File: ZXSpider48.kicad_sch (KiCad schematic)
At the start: 121 parts, among them J1 Barrel_Jack_Switch, J11 EAR/MIC, J12 KB_CONN_05, J14 RESET, J15 ZX_48K_EDGE, J17 ON/OFF, J2 JTAG, J3 9V, J5 ROM_SW, J6 M-DIN KMDGX-9S-BS-1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

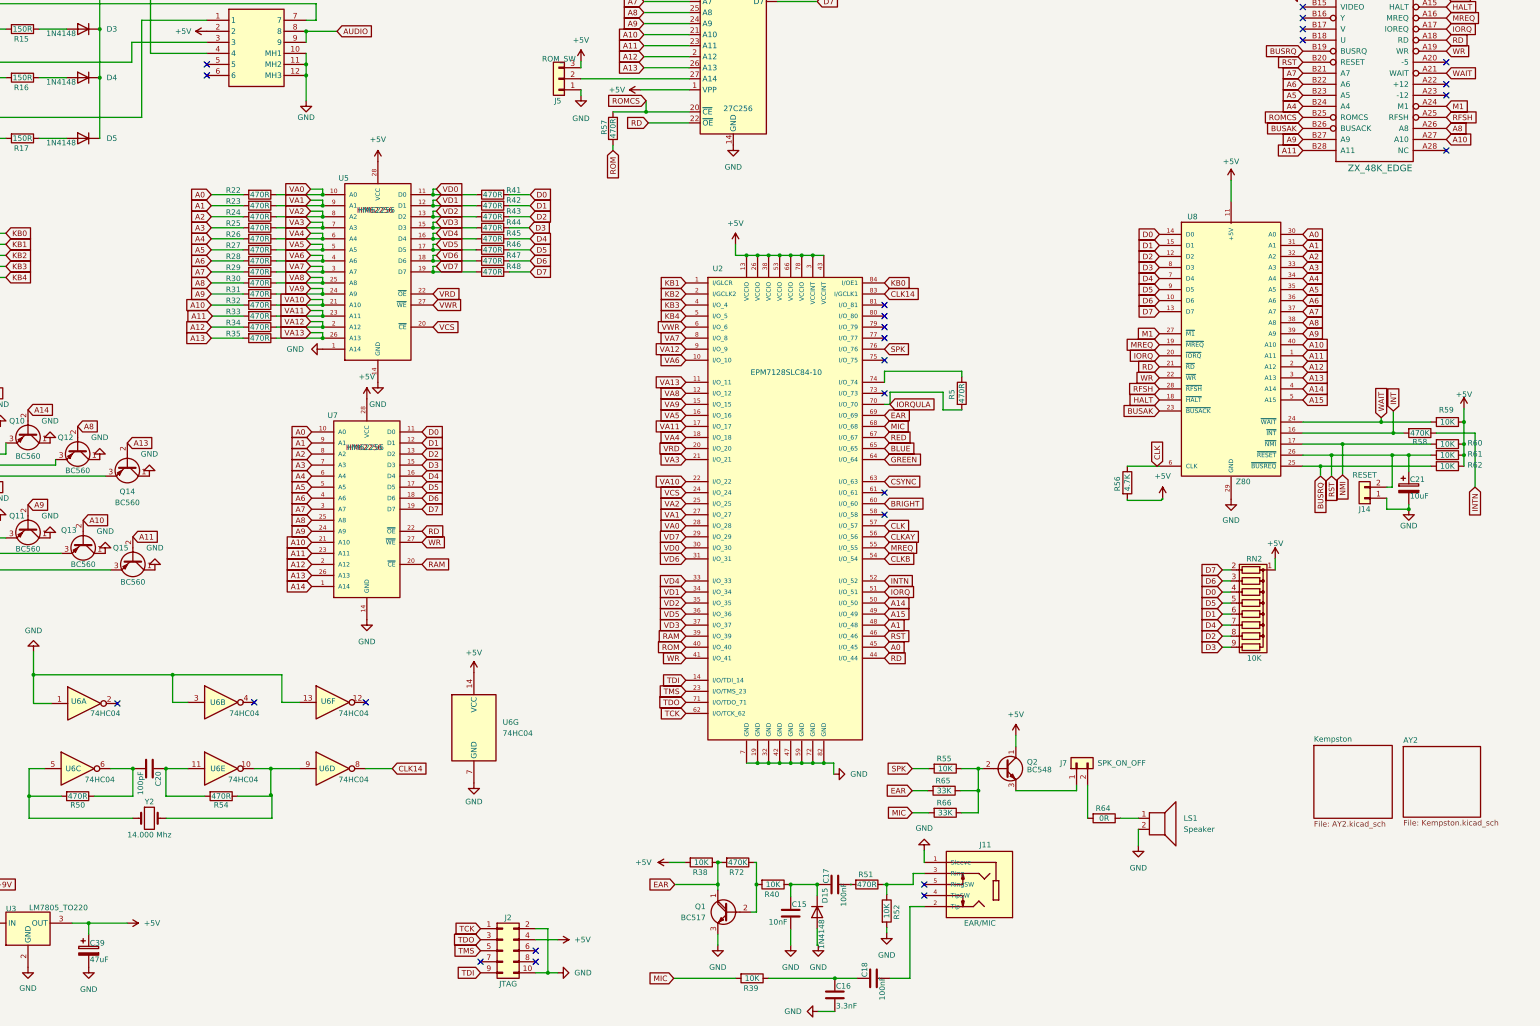
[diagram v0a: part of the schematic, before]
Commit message: Add files via upload
Added optional +/-12V for IF2 Serial support. Only fit if required.
Added jumper J18 to enable/disable Joystick interface ( fitted to enable, remove to disable).
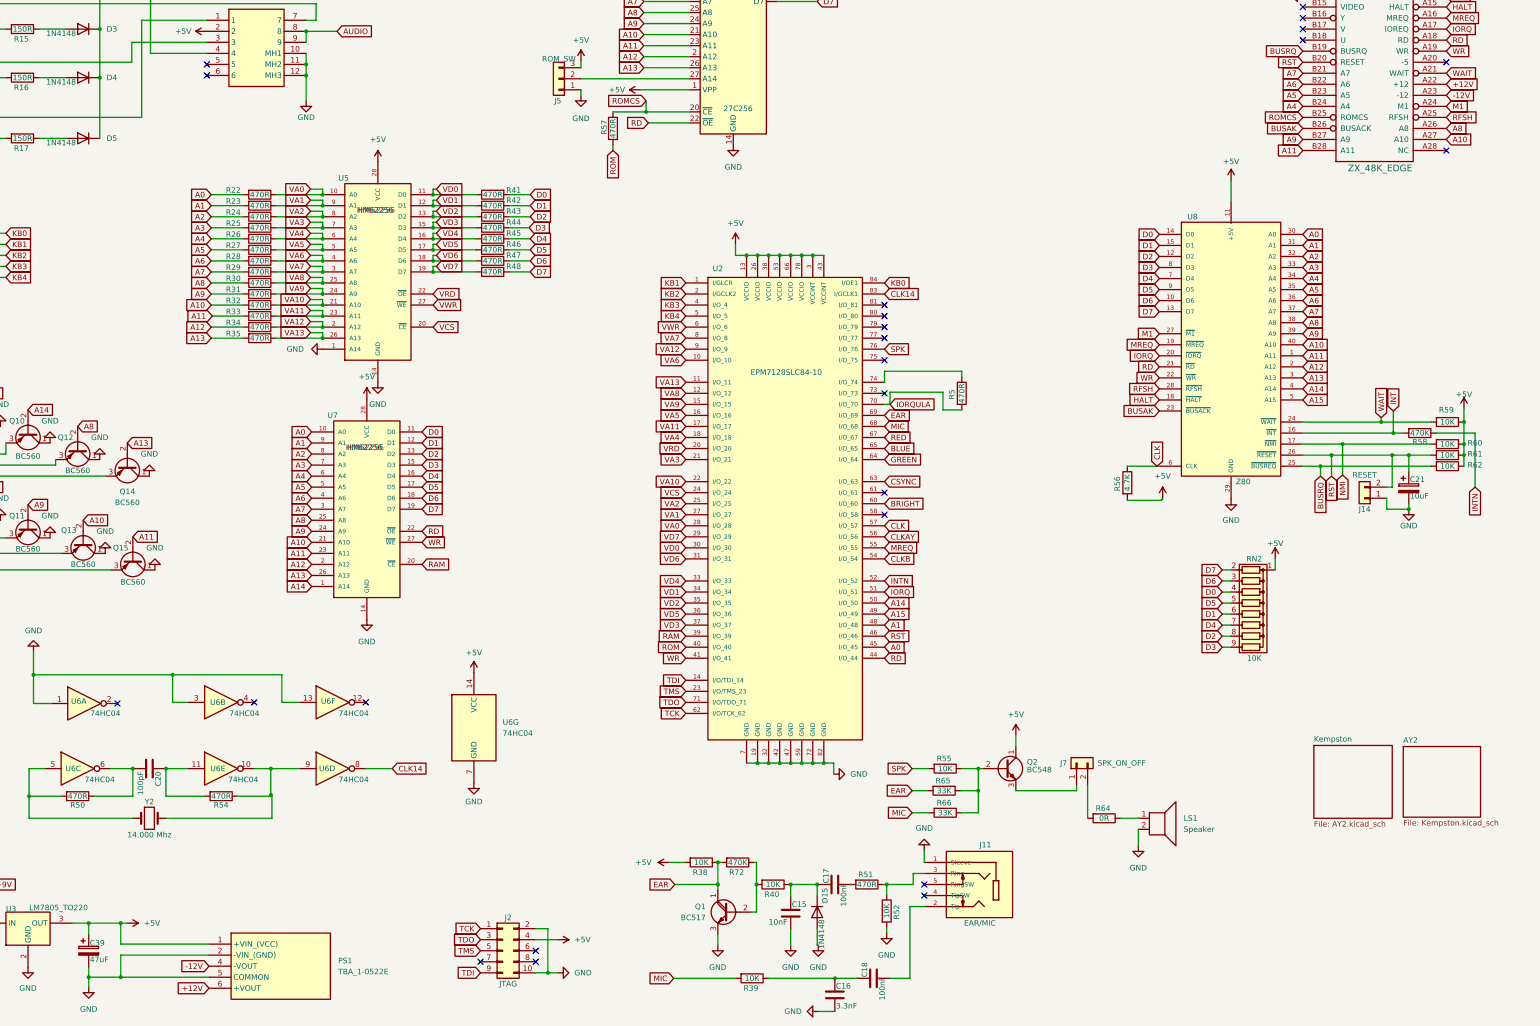
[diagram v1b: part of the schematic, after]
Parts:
- added PS1: TBA_1-0522E, _MOD:TBA10522E, symbol _Symbols:TBA_1-0522E
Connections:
- net +5V: now also PS1.1 (+VIN_(VCC))
- net GND: now also PS1.2 (-VIN_(GND)), PS1.5 (COMMON)
- net +12V: now reaches J15.A22 (+12)
- net +12V: now also PS1.6 (+VOUT)
- net -12V: now reaches J15.A23 (-12)
- net -12V: now also PS1.4 (-VOUT)
- no-connect marks 27 -> 25

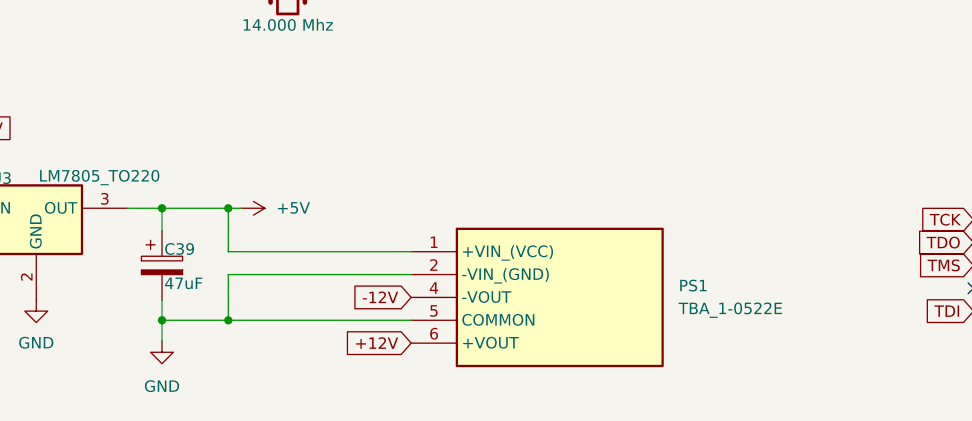
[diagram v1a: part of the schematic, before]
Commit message: Added header for AY3-8910 IOB (J18) and moved position of U1 and U4
* Routed AY3-8910 IOB Bits0-7 to header   J18 Pins  1(Bit0)- 8(Bit7)
* AY3-8910 IOA Bits 0-7 can be picked from U1 pins  7(Bit7)-14(Bit0)
* AY3-8912 IOA Bits 1-7 can be picked from U4 Pins 14(Bit7)-20(Bit1)
* AY3-8912 IOA Bit0 can be picked from J20
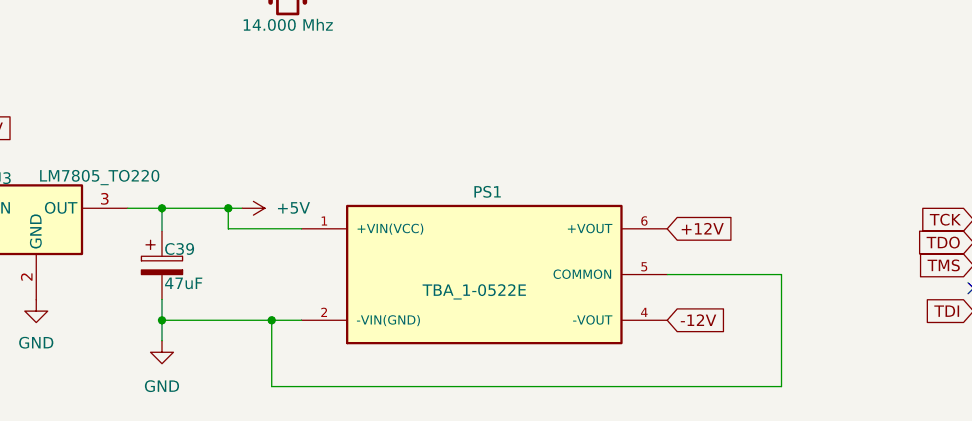
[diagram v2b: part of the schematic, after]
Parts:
- PS1: MANUFACTURER (none) -> Traco Power; MAXIMUM_PACKAGE_HEIGHT (none) -> 10.0mm; PARTREV (none) -> April 19, 2021; STANDARD (none) -> Manufacturer Recommendation
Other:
- moved on the sheet: PS1
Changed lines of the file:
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@@
 	(title_block
 		(title "ZX SPIDER 48 LBA")
-		(date "2026-06-24")
-		(rev "1.1")
+		(date "2026-06-25")
+		(rev "1.2")
 		(company "Drawn By LiveBoxAndy ")
-		(comment 1 "See ReadMe.MD for more details")
-		(comment 2 "Moved resistors from under chips and moved various components around to suit Kicad 10")
-		(comment 3 "Changed MiniDIN to 9 Pin, the same as ZX Max 128 and others. Added +/-12V option.")
+		(comment 3 "See ReadMe.MD for more details")
 		(comment 4 "Based on schematics/layout from https://github.com/konkotgit/ZX-48-Spider Rev 1.1")
 	)
@@
 	)
 	(junction
-		(at 91.186 264.16)
-		(diameter 0)
-		(color 0 0 0 0)
-	)
-	(junction
 		(at 157.48 16.51)
 		(diameter 0)
@@
 	)
 	(junction
+		(at 96.012 276.606)
+		(diameter 0)
+		(color 0 0 0 0)
+	)
+	(junction
 		(at 82.55 25.4)
 		(diameter 0)
@@
 	)
 	(junction
-		(at 91.186 276.606)
-		(diameter 0)
-		(color 0 0 0 0)
-	)
-	(junction
 		(at 93.98 228.6)
 		(diameter 0)
@@
 	)
 	(junction
+		(at 91.186 264.16)
+		(diameter 0)
+		(color 0 0 0 0)
+	)
+	(junction
 		(at 163.068 106.68)
 		(diameter 0)
@@
 	(wire
 		(pts
-			(xy 91.186 271.526) (xy 91.186 276.606)
+			(xy 96.012 283.972) (xy 96.012 276.606)
 		)
 		(stroke
@@
 	(wire
 		(pts
-			(xy 111.506 271.526) (xy 91.186 271.526)
+			(xy 96.012 283.972) (xy 152.654 283.972)
 		)
 		(stroke
@@
 	(wire
 		(pts
-			(xy 111.506 276.606) (xy 91.186 276.606)
+			(xy 99.314 276.606) (xy 96.012 276.606)
 		)
 		(stroke
@@
 	(wire
 		(pts
+			(xy 152.654 283.972) (xy 152.654 271.526)
+		)
+		(stroke
+			(width 0)
+			(type default)
+		)
+	)
+	(wire
+		(pts
 			(xy 25.4 147.574) (xy 25.4 153.67)
 		)
@@
 	(wire
 		(pts
-			(xy 91.186 276.606) (xy 83.82 276.606)
+			(xy 83.82 276.606) (xy 96.012 276.606)
 		)
 		(stroke
@@
 	(wire
 		(pts
-			(xy 91.186 268.986) (xy 91.186 264.16)
+			(xy 91.186 266.446) (xy 91.186 264.16)
 		)
 		(stroke
@@
 	(wire
 		(pts
+			(xy 152.654 271.526) (xy 139.954 271.526)
+		)
+		(stroke
+			(width 0)
+			(type default)
+		)
+	)
+	(wire
+		(pts
 			(xy 276.098 247.396) (xy 276.098 250.19)
 		)
@@
 	(wire
 		(pts
-			(xy 111.506 268.986) (xy 91.186 268.986)
+			(xy 99.314 266.446) (xy 91.186 266.446)
 		)
 		(stroke
@@
 	(global_label "-12V"
 		(shape input)
-		(at 111.506 274.066 180)
+		(at 139.954 276.606 0)
 		(fields_autoplaced yes)
 		(effects
@@
 				(size 1.27 1.27)
 			)
-			(justify right)
+			(justify left)
 		)
 		(property "Intersheetrefs" "${INTERSHEET_REFS}"
-			(at 103.4408 274.066 0)
+			(at 148.0192 276.606 0)
 			(hide yes)
 			(show_name no)
@@
 					(size 1.27 1.27)
 				)
-				(justify right)
+				(justify left)
 			)
 		)
@@
 	(global_label "+12V"
 		(shape input)
-		(at 111.506 279.146 180)
+		(at 139.954 266.446 0)
 		(fields_autoplaced yes)
 		(effects
@@
 				(size 1.27 1.27)
 			)
-			(justify right)
+			(justify left)
 		)
 		(property "Intersheetrefs" "${INTERSHEET_REFS}"
-			(at 103.4408 279.146 0)
+			(at 148.0192 266.446 0)
 			(hide yes)
 			(show_name no)
@@
 					(size 1.27 1.27)
 				)
-				(justify right)
+				(justify left)
 			)
 		)
@@
 	(symbol
 		(lib_id "_Symbols:TBA_1-0522E")
-		(at 111.506 268.986 0)
+		(at 119.634 271.526 0)
 		(unit 1)
 		(body_style 1)
@@
 		(in_pos_files yes)
 		(dnp no)
-		(fields_autoplaced yes)
 		(property "Reference" "PS1"
-			(at 141.224 272.7959 0)
+			(at 118.364 262.382 0)
 			(show_name no)
 			(do_not_autoplace no)
@@
 		)
 		(property "Value" "TBA_1-0522E"
-			(at 141.224 275.3359 0)
+			(at 112.776 273.304 0)
 			(show_name no)
 			(do_not_autoplace no)
@@
 		)
 		(property "Footprint" "_MOD:TBA10522E"
-			(at 140.716 363.906 0)
+			(at 148.844 366.446 0)
 			(hide yes)
 			(show_name no)
@@
 		)
 		(property "Datasheet" "https://tracopower.com/tba1e-datasheet/"
-			(at 140.716 463.906 0)
+			(at 148.844 466.446 0)
 			(hide yes)
 			(show_name no)
@@
 		)
 		(property "Description" "1 Watt DC/DC converter, industrial, +/-10% input, short circuit protection, unregulated, encapsulated, SIP-7"
-			(at 111.506 268.986 0)
+			(at 119.634 271.526 0)
 			(hide yes)
 			(show_name no)
@@
 		)
 		(property "Height" "10.35"
-			(at 140.716 663.906 0)
+			(at 148.844 666.446 0)
 			(hide yes)
 			(show_name no)
@@
 		)
 		(property "Mouser Part Number" "495-TBA1-0522E"
-			(at 140.716 763.906 0)
+			(at 148.844 766.446 0)
 			(hide yes)
 			(show_name no)
@@
 		)
 		(property "Mouser Price/Stock" "https://www.mouser.co.uk/ProductDetail/TRACO-Power/TBA-1-0522E?qs=byeeYqUIh0N72%2FQSgieQ2g%3D%3D"
-			(at 140.716 863.906 0)
+			(at 148.844 866.446 0)
 			(hide yes)
 			(show_name no)
@@
 		)
 		(property "Manufacturer_Name" "Traco Power"
-			(at 140.716 963.906 0)
+			(at 148.844 966.446 0)
 			(hide yes)
 			(show_name no)
@@
 		)
 		(property "Manufacturer_Part_Number" "TBA 1-0522E"
-			(at 140.716 1063.906 0)
+			(at 148.844 1066.446 0)
 			(hide yes)
 			(show_name no)
@@
 			)
 		)
+		(property "PARTREV" "April 19, 2021"
+			(at 119.634 271.526 0)
+			(hide yes)
+			(show_name no)
+			(do_not_autoplace no)
+			(effects
+				(font
+					(size 1.27 1.27)
+				)
+				(justify bottom)
+			)
+		)
+		(property "STANDARD" "Manufacturer Recommendation"
+			(at 119.634 271.526 0)
+			(hide yes)
+			(show_name no)
+			(do_not_autoplace no)
+			(effects
+				(font
+					(size 1.27 1.27)
+				)
+				(justify bottom)
+			)
+		)
+		(property "MAXIMUM_PACKAGE_HEIGHT" "10.0mm"
+			(at 119.634 271.526 0)
+			(hide yes)
+			(show_name no)
+			(do_not_autoplace no)
+			(effects
+				(font
+					(size 1.27 1.27)
+				)
+				(justify bottom)
+			)
+		)
+		(property "MANUFACTURER" "Traco Power"
+			(at 119.634 271.526 0)
+			(hide yes)
+			(show_name no)
+			(do_not_autoplace no)
+			(effects
+				(font
+					(size 1.27 1.27)
+				)
+				(justify bottom)
+			)
+		)

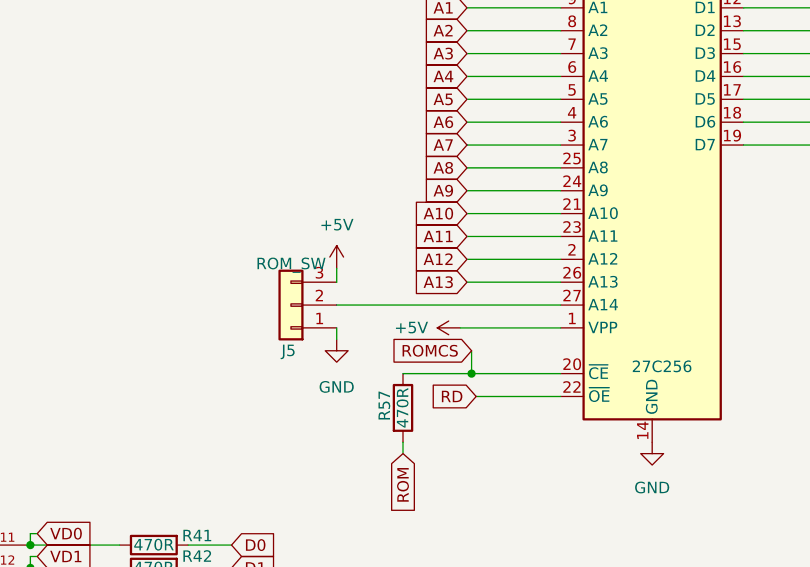
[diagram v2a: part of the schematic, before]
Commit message: Add files via upload
Changed ROM select to 2 pin rather than 3 pin header
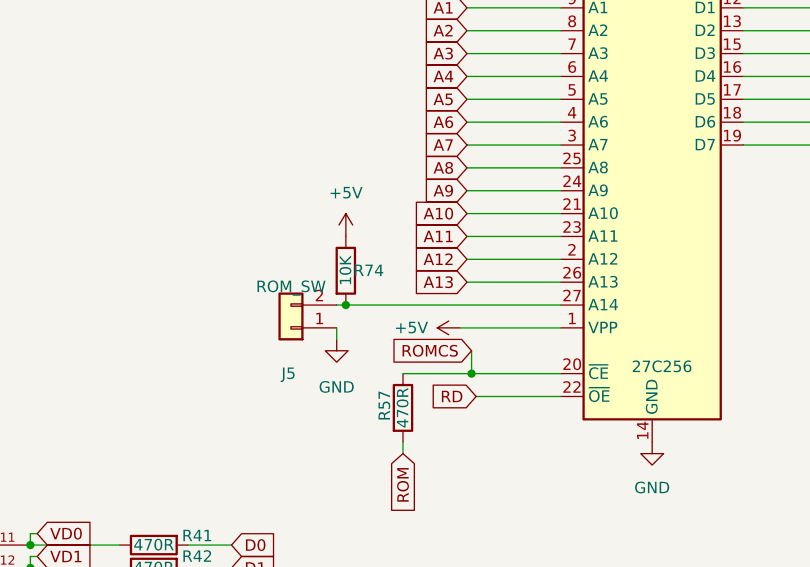
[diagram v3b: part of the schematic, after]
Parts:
- added R74: 10K, Resistor_THT:R_Axial_DIN0204_L3.6mm_D1.6mm_P7.62mm_Horizontal, symbol Device:R
- J5: footprint Connector_PinHeader_2.54mm:PinHeader_1x03_P2.54mm_Vertical -> Connector_PinHeader_2.54mm:PinHeader_1x02_P2.54mm_Vertical; symbol Connector_Generic:Conn_01x03 -> Connector_Generic:Conn_01x02
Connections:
- net +5V: now also R74.1; no longer J5.3 (Pin_3)
- net at J5.2 (Pin_2), U10.27 (A14): now also R74.2
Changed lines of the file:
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@@
 	)
 	(junction
+		(at 198.12 69.85)
+		(diameter 0)
+		(color 0 0 0 0)
+	)
+	(junction
 		(at 58.166 58.42)
 		(diameter 0)
@@
 	(wire
 		(pts
-			(xy 197.104 65.786) (xy 197.104 67.31)
-		)
-		(stroke
-			(width 0)
-			(type default)
-		)
-	)
-	(wire
-		(pts
 			(xy 137.668 95.25) (xy 137.668 96.52)
 		)
@@
 	(wire
 		(pts
+			(xy 198.12 69.85) (xy 197.104 69.85)
+		)
+		(stroke
+			(width 0)
+			(type default)
+		)
+	)
+	(wire
+		(pts
 			(xy 137.668 97.79) (xy 137.668 99.06)
 		)
@@
 	(wire
 		(pts
-			(xy 221.996 69.85) (xy 197.104 69.85)
+			(xy 221.996 69.85) (xy 198.12 69.85)
 		)
 		(stroke
@@
 	(symbol
 		(lib_id "power:+5V")
-		(at 197.104 65.786 0)
+		(at 198.12 62.23 0)
 		(unit 1)
 		(body_style 1)
@@
 		(fields_autoplaced yes)
 		(property "Reference" "#PWR080"
-			(at 197.104 69.596 0)
+			(at 198.12 66.04 0)
 			(hide yes)
 			(show_name no)
@@
 		)
 		(property "Value" "+5V"
-			(at 197.104 60.96 0)
+			(at 198.12 57.404 0)
 			(show_name no)
 			(do_not_autoplace no)
@@
 		)
 		(property "Footprint" ""
-			(at 197.104 65.786 0)
+			(at 198.12 62.23 0)
 			(hide yes)
 			(show_name no)
@@
 		)
 		(property "Datasheet" ""
-			(at 197.104 65.786 0)
+			(at 198.12 62.23 0)
 			(hide yes)
 			(show_name no)
@@
 		)
 		(property "Description" "Power symbol creates a global label with name \"+5V\""
-			(at 197.104 65.786 0)
+			(at 198.12 62.23 0)
 			(hide yes)
 			(show_name no)
@@
 	)
 	(symbol
-		(lib_id "Connector_Generic:Conn_01x03")
-		(at 192.024 69.85 180)
+		(lib_id "Connector_Generic:Conn_01x02")
+		(at 192.024 72.39 180)
 		(unit 1)
 		(body_style 1)
@@
 		(dnp no)
 		(property "Reference" "J5"
-			(at 191.77 74.93 0)
+			(at 191.77 77.47 0)
 			(show_name no)
 			(do_not_autoplace no)
@@
 		)
 		(property "Value" "ROM_SW"
-			(at 192.024 65.278 0)
+			(at 192.024 67.818 0)
 			(show_name no)
 			(do_not_autoplace no)
@@
 			)
 		)
-		(property "Footprint" "Connector_PinHeader_2.54mm:PinHeader_1x03_P2.54mm_Vertical"
-			(at 192.024 69.85 0)
+		(property "Footprint" "Connector_PinHeader_2.54mm:PinHeader_1x02_P2.54mm_Vertical"
+			(at 192.024 72.39 0)
 			(hide yes)
 			(show_name no)
@@
 		)
 		(property "Datasheet" ""
-			(at 192.024 69.85 0)
+			(at 192.024 72.39 0)
 			(hide yes)
 			(show_name no)
@@
 		)
 		(property "Description" "Generic connector, single row, 01x03, script generated (kicad-library-utils/schlib/autogen/connector/)"
-			(at 192.024 69.85 0)
+			(at 192.024 72.39 0)
 			(hide yes)
 			(show_name no)
@@
 		(pin "2"
 		)
-		(pin "3"
-		)
 		(pin "1"
 		)
@@
 					(unit 1)
 				)
+			)
+		)
+	)
+	(symbol
+		(lib_id "Device:R")
+		(at 198.12 66.04 0)
+		(unit 1)
+		(body_style 1)
+		(exclude_from_sim no)
+		(in_bom yes)
+		(on_board yes)
+		(in_pos_files yes)
+		(dnp no)
+		(property "Reference" "R74"
+			(at 200.66 66.04 0)
+			(show_name no)
+			(do_not_autoplace no)
+			(effects
+				(font
+					(size 1.27 1.27)
+				)
+			)
+		)
+		(property "Value" "10K"
+			(at 198.12 66.04 90)
+			(show_name no)
+			(do_not_autoplace no)
+			(effects
+				(font
+					(size 1.27 1.27)
+				)
+			)
+		)
+		(property "Footprint" "Resistor_THT:R_Axial_DIN0204_L3.6mm_D1.6mm_P7.62mm_Horizontal"
+			(at 196.342 66.04 90)
+			(hide yes)
+			(show_name no)
+			(do_not_autoplace no)
+			(effects
+				(font
+					(size 1.27 1.27)
+				)
+			)
+		)
+		(property "Datasheet" ""
+			(at 198.12 66.04 0)
+			(hide yes)
+			(show_name no)
+			(do_not_autoplace no)
+			(effects
+				(font
+					(size 1.27 1.27)
+				)
+			)
+		)
+		(property "Description" "Resistor"
+			(at 198.12 66.04 0)
+			(hide yes)
+			(show_name no)
+			(do_not_autoplace no)
+			(effects
+				(font
+					(size 1.27 1.27)
+				)
+			)
+		)
+		(pin "2"
+		)
+		(pin "1"
+		)
+		(instances
+			(project "ZXSpider48"
+				(path "/c8dee8da-cc77-415a-9e31-9e236c26c0e6"
+					(reference "R74")
+					(unit 1)
+				)
